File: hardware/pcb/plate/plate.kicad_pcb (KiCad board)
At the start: 2 copper layers, 133 x 122 mm, 52 parts

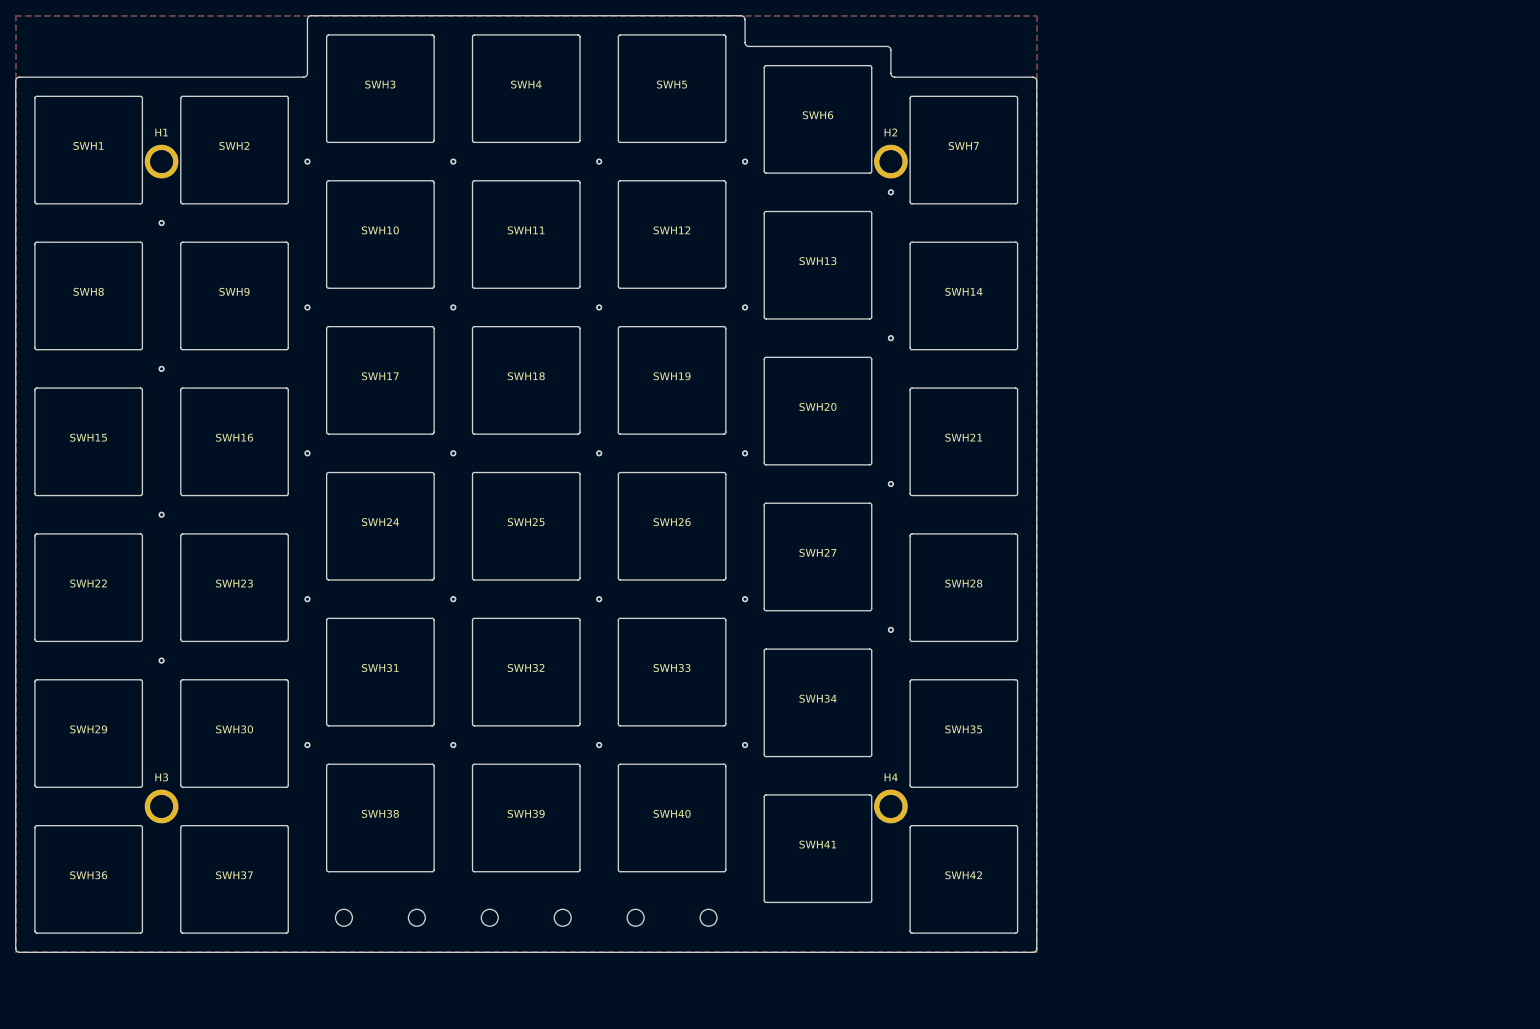
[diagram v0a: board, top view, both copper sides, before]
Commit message: merge
hw:
- fix sch
- fix plate
- rename to fercus-dongle-usb-a

doc:
- add assembly
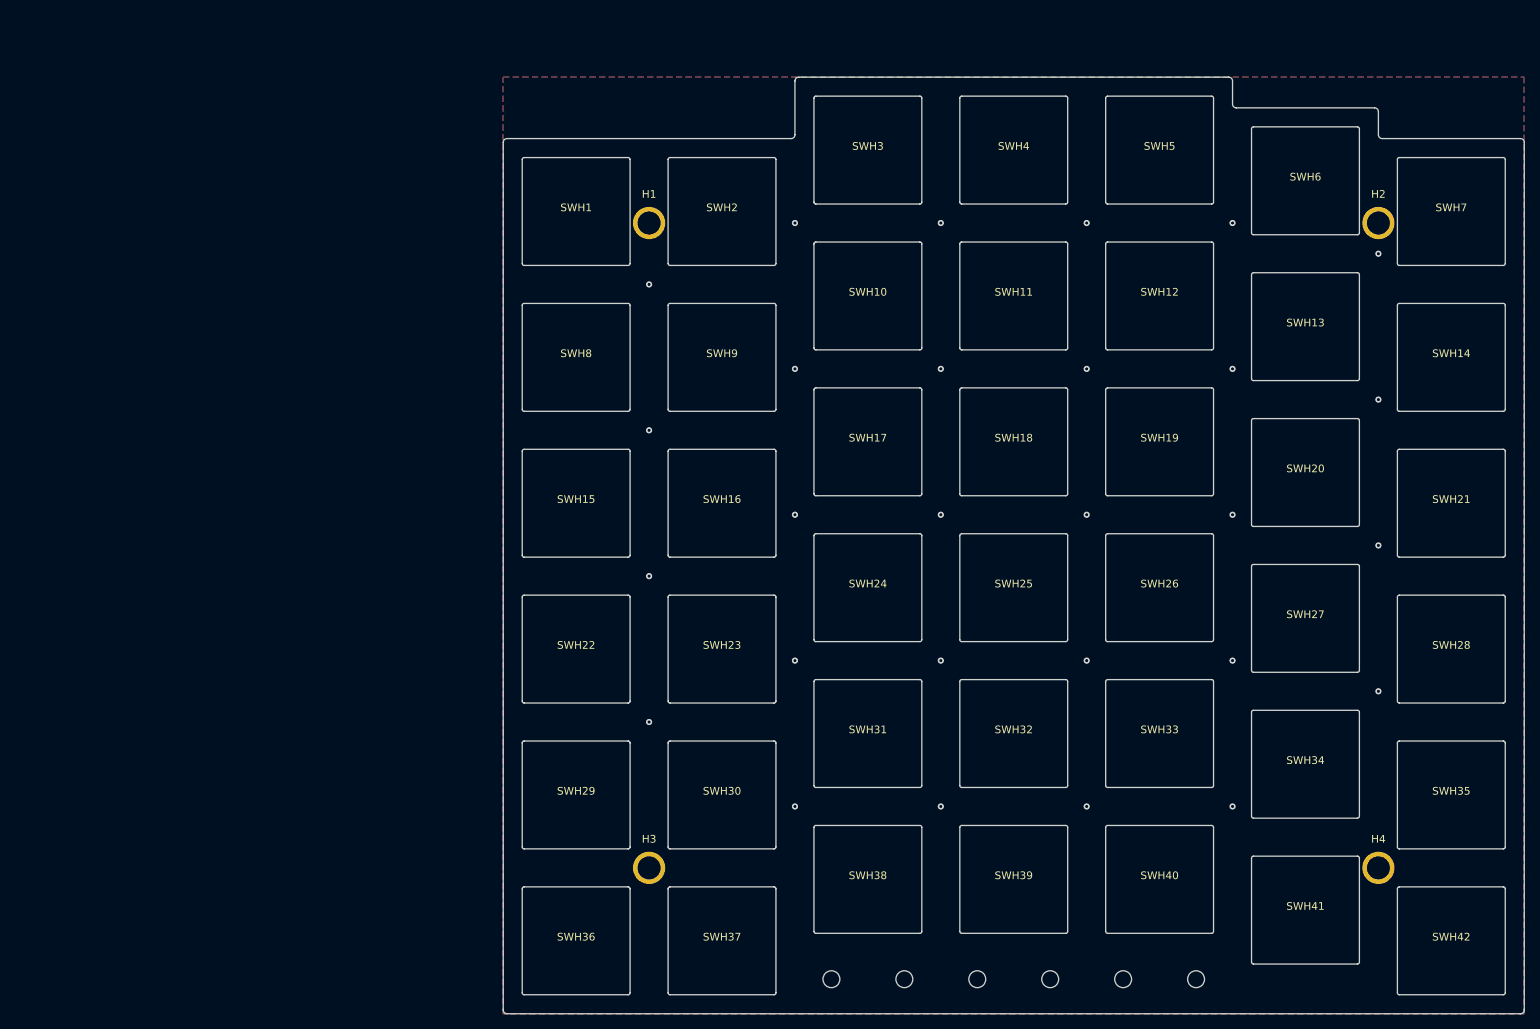
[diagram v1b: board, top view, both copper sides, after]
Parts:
- H1, H2, H3, H4: footprint chulaine:MountingHole_3.0mm_M3_Pad4.4mm -> chulaine:MountingHole_3.0mm_M3_Pad4.2mm
- SWH1, SWH10, SWH11, SWH12, SWH13, SWH14, SWH15, SWH16, SWH17, SWH18, SWH19, SWH2, SWH20, SWH21, SWH22, SWH23, SWH24, SWH25, SWH26, SWH27, SWH28, SWH29, SWH3, SWH30, SWH31, SWH32, SWH33, SWH34, SWH35, SWH36, SWH37, SWH38, SWH39, SWH4, SWH40, SWH41, SWH42, SWH5, SWH6, SWH7, SWH8, SWH9: footprint chulaine:SW_RAESHA_Low_Profile_Optical_Plate -> chulaine:SW_RAESHA_Low_Profile_Optical_Plate_14.05mm
- moved H1 64.0 mm to (102.5, 47.0)
- moved H11 64.0 mm to (164.2, 145.5)
- moved H12 64.0 mm to (173.8, 145.5)
- moved H2 64.0 mm to (197.5, 47.0)
- moved H3 64.0 mm to (102.5, 131.0)
- moved H4 64.0 mm to (197.5, 131.0)
- moved H5 64.0 mm to (126.2, 145.5)
- moved H6 64.0 mm to (135.8, 145.5)
- moved H7 64.0 mm to (145.2, 145.5)
- moved H8 64.0 mm to (154.8, 145.5)
- moved SWH1 64.0 mm to (93.0, 45.5)
- moved SWH10 64.0 mm to (131.0, 56.5)
- moved SWH11 64.0 mm to (150.0, 56.5)
- moved SWH12 64.0 mm to (169.0, 56.5)
- moved SWH13 64.0 mm to (188.0, 60.5)
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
